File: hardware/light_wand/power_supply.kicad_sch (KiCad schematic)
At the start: 14 parts

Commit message: got backup adx working
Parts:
- added U2: ~, symbol light_wand_library:S-82K1BAM-I6T1U
- L1: value L -> 6.8uH
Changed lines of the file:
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@@
+    )
+  )
+  (symbol (lib_id "light_wand_library:S-82K1BAM-I6T1U") (at 59.69 67.31 0) (unit 1)
+    (in_bom yes) (on_board yes) (dnp no) (fields_autoplaced)
+    (property "Reference" "U2" (at 59.69 58.42 0)
+      (effects (font (size 1.27 1.27)))
+    )
+    (property "Value" "~" (at 59.69 67.31 0)
+      (effects (font (size 1.27 1.27)))
+    )
+    (property "Footprint" "" (at 59.69 67.31 0)
+      (effects (font (size 1.27 1.27)) hide)
+    )
+    (property "Datasheet" "" (at 59.69 67.31 0)
+      (effects (font (size 1.27 1.27)) hide)
+    )
+    (pin "1")
+    (pin "2")
+    (pin "3")
+    (pin "4")
+    (pin "5")
+    (pin "6")
+    (instances
+      (project "light_wand"
+        (path "/1490551a-2c24-45df-b317-45d6c7f84af9/1ba98658-464e-4305-848f-5f718e928d99"
+          (reference "U2") (unit 1)
+        )
+      )
     )
   )
@@
       (effects (font (size 1.27 1.27)))
     )
-    (property "Value" "L" (at 167.64 40.64 90)
-      (effects (font (size 1.27 1.27)))
-    )
+    (property "Value" "6.8uH" (at 167.64 40.64 90)
+      (effects (font (size 1.27 1.27)))
+    )

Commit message: Tested boost converter
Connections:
- net at C1.1, C2.1, L1.1: now also C3.1, U1.2 (VIN), U1.3 (EN)
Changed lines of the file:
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@@
 (kicad_sch (version 20230121) (generator eeschema)
   (paper "A4")
+  (junction (at 146.05 43.18) (diameter 0) (color 0 0 0 0)
+  )
   (junction (at 212.09 43.18) (diameter 0) (color 0 0 0 0)
   )
@@
   )
   (junction (at 198.12 63.5) (diameter 0) (color 0 0 0 0)
+  )
+  (junction (at 146.05 63.5) (diameter 0) (color 0 0 0 0)
   )
   (junction (at 154.94 66.04) (diameter 0) (color 0 0 0 0)
@@
   )
   (wire (pts (xy 226.06 43.18) (xy 212.09 43.18))
+    (stroke (width 0) (type default))
+  )
+  (wire (pts (xy 146.05 63.5) (xy 134.62 63.5))
+    (stroke (width 0) (type default))
+  )
+  (wire (pts (xy 146.05 43.18) (xy 163.83 43.18))
     (stroke (width 0) (type default))
   )
@@
     (stroke (width 0) (type default))
   )
+  (wire (pts (xy 146.05 43.18) (xy 146.05 63.5))
+    (stroke (width 0) (type default))
+  )
   (wire (pts (xy 158.75 58.42) (xy 157.48 58.42))
     (stroke (width 0) (type default))
@@
     (stroke (width 0) (type default))
   )
-  (wire (pts (xy 154.94 63.5) (xy 134.62 63.5))
+  (wire (pts (xy 154.94 63.5) (xy 146.05 63.5))
     (stroke (width 0) (type default))
   )
@@
     (stroke (width 0) (type default))
   )
-  (wire (pts (xy 135.89 43.18) (xy 163.83 43.18))
+  (wire (pts (xy 135.89 43.18) (xy 146.05 43.18))
     (stroke (width 0) (type default))
   )

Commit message: Finished schematic layout for power supply
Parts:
- removed U2: ~, symbol light_wand_library:S-82K1BAM-I6T1U
- added C9: 0.1uF, symbol Device:C
- added J1: BatteryPlus, Connector_Wire:SolderWire-0.1sqmm_1x01_D0.4mm_OD1mm_Relief, symbol Connector_Generic:Conn_01x01
- added J2: BatteryMinus, Connector_Wire:SolderWire-0.1sqmm_1x01_D0.4mm_OD1mm_Relief, symbol Connector_Generic:Conn_01x01
- added R4: 470, symbol Device:R
- added R5: 1.5m, symbol Device:R
- added R6: 330, symbol Device:R
- added U2: ~, symbol light_wand_library:Si3900DV
- added U3: ~, symbol light_wand_library:S-82K1BAM-I6T1U
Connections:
- net GND: now also R4.1, U2.2 (S2)
- net at C1.1, C2.1, C3.1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: now also J1.1 (Pin_1), R6.2
- new net: C9.1, R6.1, U3.5 (VDD)
- new net: C9.2, J2.1 (Pin_1), R5.2, U3.4 (VSS)
- new net: U2.1 (G1), U3.3 (DO)
- new net: U2.3 (G2), U3.2 (CO)
- new net: U2.4 (D2), U2.6 (D1)
- new net: R5.1, U2.5 (S1), U3.6 (VINI)
- new net: R4.2, U3.1 (VM)
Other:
- note added: "Battery protection"
- note added: "Boost converter"
- note added: "Li-ion Power Supply for the Light Wand"
- note removed: "LiPo Power Supply for the Light Wand"

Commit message: Added footprint for battery prot ic
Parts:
- removed J1: BatteryPlus, Connector_Wire:SolderWire-0.1sqmm_1x01_D0.4mm_OD1mm_Relief, symbol Connector_Generic:Conn_01x01
- removed J2: BatteryMinus, Connector_Wire:SolderWire-0.1sqmm_1x01_D0.4mm_OD1mm_Relief, symbol Connector_Generic:Conn_01x01
- U2: footprint (none) -> Package_SO:TSOP-6_1.65x3.05mm_P0.95mm
- U3: footprint (none) -> light_wand_footprints:HSNT-6
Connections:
- net Vin-: now reaches C9.2, R5.2, U3.4 (VSS)
- net Vin+: now reaches C1.1, C2.1, C3.1, L1.1, R6.2, U1.2 (VIN), U1.3 (EN)
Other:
- note added: "Connect battery here"
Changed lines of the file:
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@@
   (junction (at 177.8 43.18) (diameter 0) (color 0 0 0 0)
   )
+  (junction (at 135.89 43.18) (diameter 0) (color 0 0 0 0)
+  )
+  (junction (at 198.12 43.18) (diameter 0) (color 0 0 0 0)
+  )
+  (junction (at 198.12 63.5) (diameter 0) (color 0 0 0 0)
+  )
+  (junction (at 87.63 120.65) (diameter 0) (color 0 0 0 0)
+  )
+  (junction (at 77.47 120.65) (diameter 0) (color 0 0 0 0)
+  )
+  (junction (at 146.05 63.5) (diameter 0) (color 0 0 0 0)
+  )
+  (junction (at 154.94 66.04) (diameter 0) (color 0 0 0 0)
+  )
+  (junction (at 92.71 120.65) (diameter 0) (color 0 0 0 0)
+  )
+  (junction (at 154.94 63.5) (diameter 0) (color 0 0 0 0)
+  )
+  (junction (at 123.19 43.18) (diameter 0) (color 0 0 0 0)
+  )
+  (junction (at 27.94 105.41) (diameter 0) (color 0 0 0 0)
+  )
+  (junction (at 226.06 43.18) (diameter 0) (color 0 0 0 0)
+  )
   (junction (at 105.41 107.95) (diameter 0) (color 0 0 0 0)
   )
-  (junction (at 135.89 43.18) (diameter 0) (color 0 0 0 0)
-  )
-  (junction (at 198.12 43.18) (diameter 0) (color 0 0 0 0)
-  )
-  (junction (at 198.12 63.5) (diameter 0) (color 0 0 0 0)
-  )
-  (junction (at 87.63 120.65) (diameter 0) (color 0 0 0 0)
-  )
-  (junction (at 77.47 120.65) (diameter 0) (color 0 0 0 0)
-  )
-  (junction (at 92.71 120.65) (diameter 0) (color 0 0 0 0)
-  )
-  (junction (at 146.05 63.5) (diameter 0) (color 0 0 0 0)
-  )
-  (junction (at 154.94 66.04) (diameter 0) (color 0 0 0 0)
-  )
-  (junction (at 154.94 63.5) (diameter 0) (color 0 0 0 0)
-  )
-  (junction (at 123.19 43.18) (diameter 0) (color 0 0 0 0)
-  )
-  (junction (at 27.94 105.41) (diameter 0) (color 0 0 0 0)
-  )
-  (junction (at 226.06 43.18) (diameter 0) (color 0 0 0 0)
-  )
   (wire (pts (xy 212.09 43.18) (xy 198.12 43.18))
     (stroke (width 0) (type default))
@@
     (stroke (width 0) (type default))
   )
-  (wire (pts (xy 92.71 120.65) (xy 107.95 120.65))
+  (wire (pts (xy 105.41 107.95) (xy 109.22 107.95))
     (stroke (width 0) (type default))
   )
@@
     (stroke (width 0) (type default))
   )
+  (wire (pts (xy 92.71 120.65) (xy 109.22 120.65))
+    (stroke (width 0) (type default))
+  )
   (wire (pts (xy 149.86 87.63) (xy 154.94 87.63))
     (stroke (width 0) (type default))
@@
     (stroke (width 0) (type default))
   )
-  (wire (pts (xy 107.95 107.95) (xy 105.41 107.95))
-    (stroke (width 0) (type default))
-  )
   (wire (pts (xy 77.47 120.65) (xy 77.47 105.41))
     (stroke (width 0) (type default))
   )
   (text "Boost converter" (at 170.18 30.48 0)
-    (effects (font (size 1.27 1.27)) (justify left bottom))
+    (effects (font (size 1.27 1.27) (thickness 0.254) bold) (justify left bottom))
   )
   (text "20204/03/04" (at 207.01 194.31 0)
@@
     (effects (font (size 1.27 1.27)) (justify left bottom))
   )
+  (text "Connect battery here" (at 106.68 115.57 0)
+    (effects (font (size 1.27 1.27)) (justify left bottom))
+  )
   (text "Battery protection" (at 53.34 92.71 0)
-    (effects (font (size 1.27 1.27)) (justify left bottom))
+    (effects (font (size 1.27 1.27) (thickness 0.254) bold) (justify left bottom))
   )
   (text "0" (at 269.24 194.31 0)
     (effects (font (size 1.27 1.27)) (justify left bottom))
   )
-  (global_label "Vout" (shape input) (at 234.95 43.18 0) (fields_autoplaced)
+  (hierarchical_label "Vout" (shape output) (at 234.95 43.18 0) (fields_autoplaced)
     (effects (font (size 1.27 1.27)) (justify left))
-    (property "Intersheetrefs" "${INTERSHEET_REFS}" (at 242.0475 43.18 0)
-      (effects (font (size 1.27 1.27)) (justify left) hide)
-    )
+  )
+  (hierarchical_label "Vin-" (shape input) (at 109.22 120.65 0) (fields_autoplaced)
+    (effects (font (size 1.27 1.27)) (justify left))
+  )
+  (hierarchical_label "Vin+" (shape input) (at 109.22 107.95 0) (fields_autoplaced)
+    (effects (font (size 1.27 1.27)) (justify left))
   )
   (symbol (lib_id "power:GND") (at 149.86 53.34 0) (unit 1)
@@
       (effects (font (size 1.27 1.27)))
     )
-    (property "Footprint" "" (at 39.37 120.65 0)
+    (property "Footprint" "Package_SO:TSOP-6_1.65x3.05mm_P0.95mm" (at 39.37 120.65 0)
       (effects (font (size 1.27 1.27)) hide)
     )
@@
     )
   )
-  (symbol (lib_id "Connector_Generic:Conn_01x01") (at 113.03 120.65 0) (unit 1)
-    (in_bom yes) (on_board yes) (dnp no) (fields_autoplaced)
-    (property "Reference" "J2" (at 115.57 119.38 0)
-      (effects (font (size 1.27 1.27)) (justify left))
-    )
-    (property "Value" "BatteryMinus" (at 115.57 121.92 0)
-      (effects (font (size 1.27 1.27)) (justify left))
-    )
-    (property "Footprint" "Connector_Wire:SolderWire-0.1sqmm_1x01_D0.4mm_OD1mm_Relief" (at 113.03 120.65 0)
-      (effects (font (size 1.27 1.27)) hide)
-    )
-    (property "Datasheet" "~" (at 113.03 120.65 0)
-      (effects (font (size 1.27 1.27)) hide)
-    )
-    (pin "1")
-    (instances
-      (project "light_wand"
-        (path "/1490551a-2c24-45df-b317-45d6c7f84af9/1ba98658-464e-4305-848f-5f718e928d99"
-          (reference "J2") (unit 1)
-        )
-      )
-    )
-  )
   (symbol (lib_id "power:GND") (at 149.86 87.63 0) (unit 1)
     (in_bom yes) (on_board yes) (dnp no) (fields_autoplaced)
@@
         (path "/1490551a-2c24-45df-b317-45d6c7f84af9/1ba98658-464e-4305-848f-5f718e928d99"
           (reference "C6") (unit 1)
-        )
-      )
-    )
-  )
-  (symbol (lib_id "Connector_Generic:Conn_01x01") (at 113.03 107.95 0) (unit 1)
-    (in_bom yes) (on_board yes) (dnp no) (fields_autoplaced)
-    (property "Reference" "J1" (at 115.57 106.68 0)
-      (effects (font (size 1.27 1.27)) (justify left))
-    )
-    (property "Value" "BatteryPlus" (at 115.57 109.22 0)
-      (effects (font (size 1.27 1.27)) (justify left))
-    )
-    (property "Footprint" "Connector_Wire:SolderWire-0.1sqmm_1x01_D0.4mm_OD1mm_Relief" (at 113.03 107.95 0)
-      (effects (font (size 1.27 1.27)) hide)
-    )
-    (property "Datasheet" "~" (at 113.03 107.95 0)
-      (effects (font (size 1.27 1.27)) hide)
-    )
-    (pin "1")
-    (instances
-      (project "light_wand"
-        (path "/1490551a-2c24-45df-b317-45d6c7f84af9/1ba98658-464e-4305-848f-5f718e928d99"
-          (reference "J1") (unit 1)
         )
       )
@@
       (effects (font (size 1.27 1.27)))
     )
-    (property "Footprint" "" (at 63.5 109.22 0)
-      (effects (font (size 1.27 1.27)) hide)
-    )
+    (property "Footprint" "light_wand_footprints:HSNT-6" (at 63.5 109.22 0)
+      (effects (font (size 1.27 1.27)) hide)
+    )

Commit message: Finished footprints for all ICs
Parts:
- U1: footprint Package_SO:SOP-8_3.9x4.9mm_P1.27mm -> light_wand_footprints:SOP-8-EP_3.9x4.9mm_P1.27mm
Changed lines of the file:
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@@
       (effects (font (size 1.27 1.27)))
     )
-    (property "Footprint" "Package_SO:SOP-8_3.9x4.9mm_P1.27mm" (at 167.64 62.23 0)
+    (property "Footprint" "light_wand_footprints:SOP-8-EP_3.9x4.9mm_P1.27mm" (at 167.64 62.23 0)
       (effects (font (size 1.27 1.27)) hide)
     )

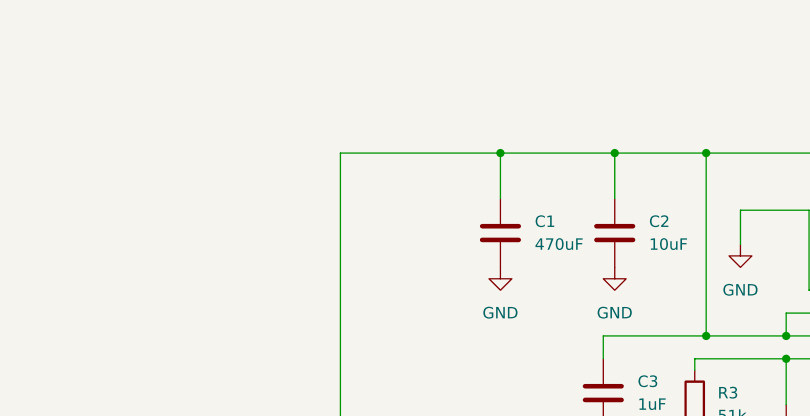
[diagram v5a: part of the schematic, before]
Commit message: Tested boost converter with dissapointing results
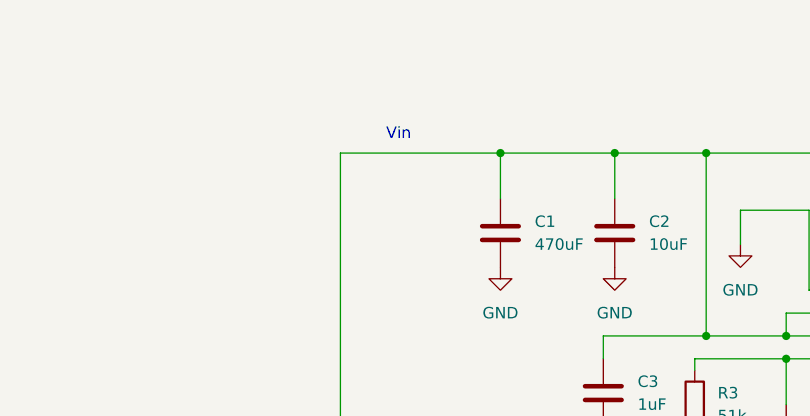
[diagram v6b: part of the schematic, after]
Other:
- note added: "Vin"
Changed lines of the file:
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@@
+    (effects (font (size 1.27 1.27)) (justify left bottom))
+  )
+  (text "Vin" (at 110.49 41.91 0)
     (effects (font (size 1.27 1.27)) (justify left bottom))
   )

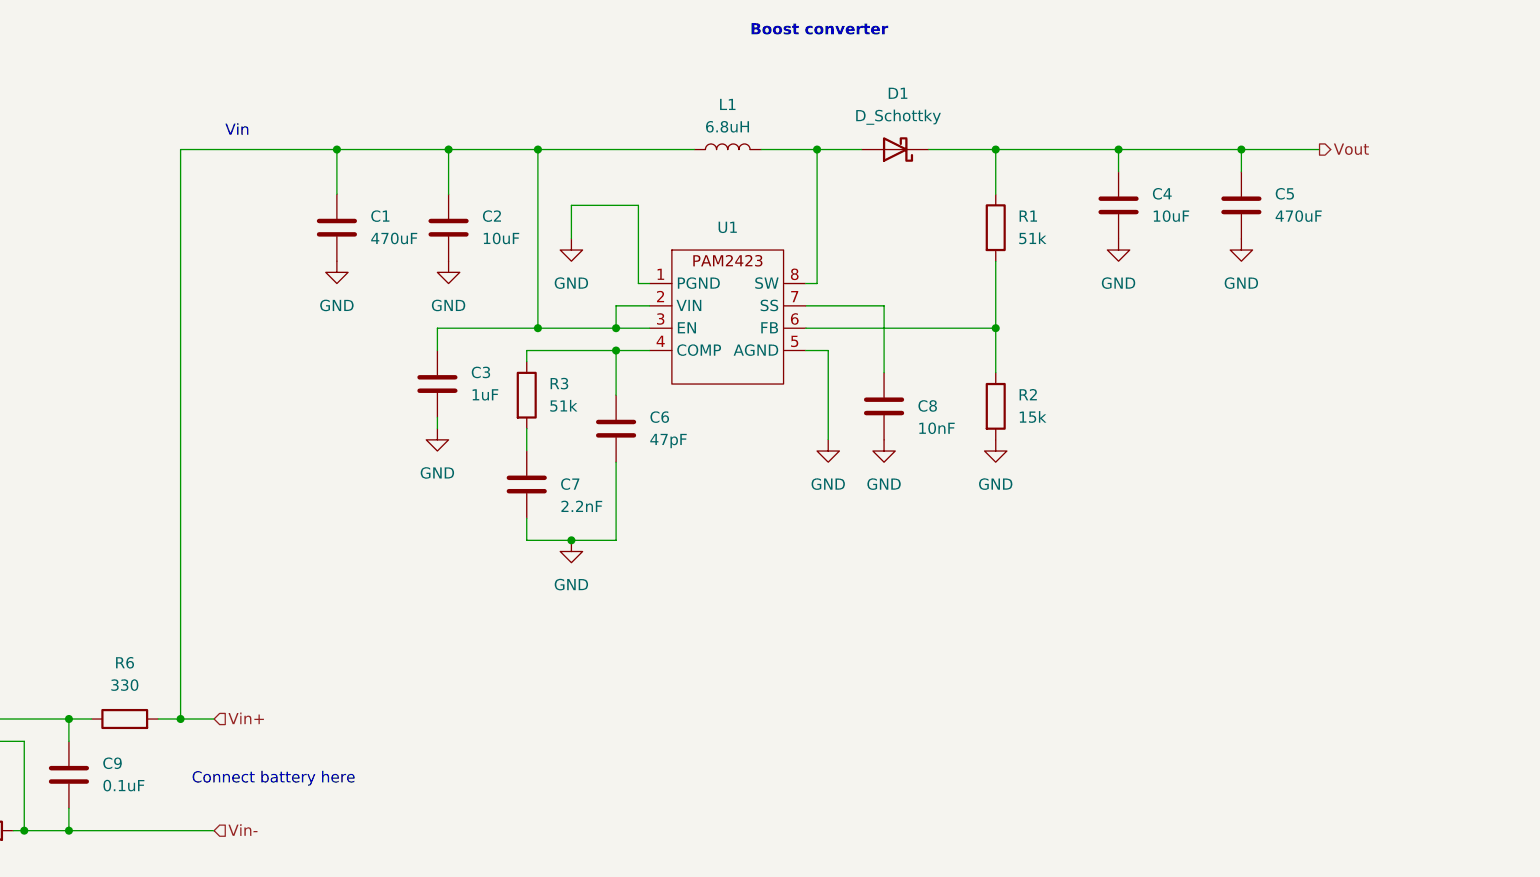
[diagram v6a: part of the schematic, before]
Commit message: Layed out schematic of the new boost converter design
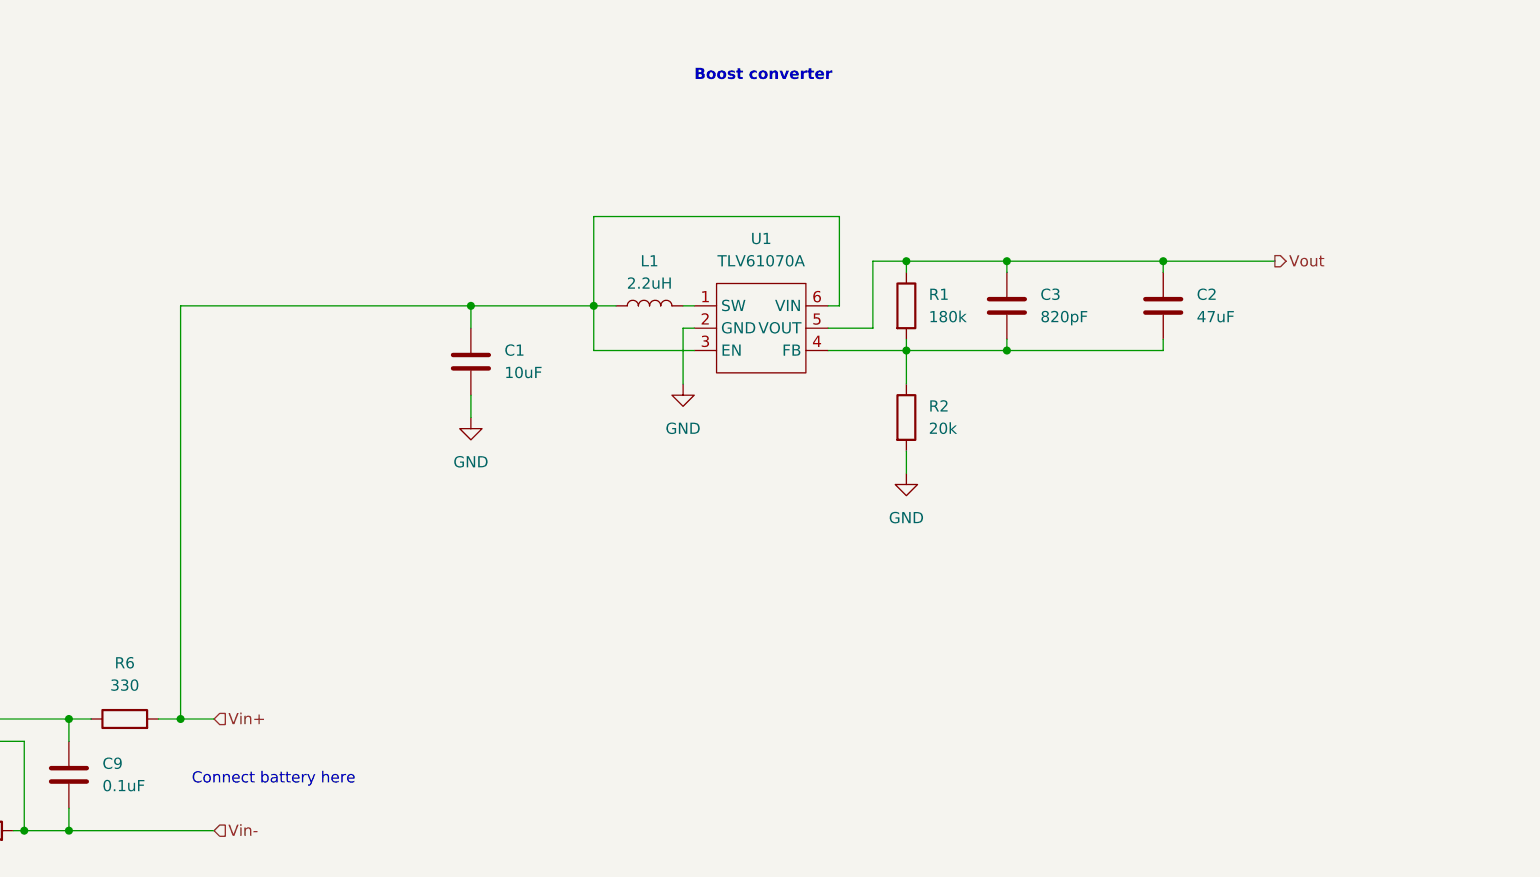
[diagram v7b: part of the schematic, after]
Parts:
- removed C4: 10uF, symbol Device:C
- removed C5: 470uF, symbol Device:C
- removed C6: 47pF, symbol Device:C
- removed C7: 2.2nF, symbol Device:C
- removed C8: 10nF, symbol Device:C
- removed D1: D_Schottky, symbol Device:D_Schottky
- removed R3: 51k, symbol Device:R
- removed U1: ~, light_wand_footprints:SOP-8-EP_3.9x4.9mm_P1.27mm, symbol light_wand_library:PAM2423
- added U1: TLV61070A, Package_TO_SOT_SMD:SOT-23-6_Handsoldering, symbol light_wand_library:TLV61070A
- C1: value 470uF -> 10uF
- C2: value 10uF -> 47uF
- C3: value 1uF -> 820pF
- L1: value 6.8uH -> 2.2uH; footprint (none) -> light_wand_footprints:74438357022_4.1x3.1mm_Inductor
- R1: value 51k -> 180k
- R2: value 15k -> 20k
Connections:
- net GND: now also U1.2 (GND); no longer C2.2, C3.2
- net Vin+: now also U1.3 (EN), U1.6 (VIN); no longer C2.1, C3.1
- net Vout: now also C2.1, C3.1, U1.5 (VOUT)
- net at L1.2: now also U1.1 (SW)
- net at R1.2, R2.1: now also C2.2, C3.2, U1.4 (FB)
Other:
- note removed: "Vin"
